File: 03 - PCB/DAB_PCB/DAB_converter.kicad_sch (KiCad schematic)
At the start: 190 parts, among them IC1 UCC27288DR, IC10 INA201AID, IC11 INA201AID, IC12 MCP6241-E_P, IC13 MCP6241-E_P, IC2 UCC27288DR, IC3 UCC27288DR, IC4 UCC27288DR, IC5 UA78L12ACDR, IC6 INA201AID, IC9 INA201AID, J3 N3431-6302RB

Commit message: started routing
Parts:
- added TP19: V', DAB:test point 2, symbol DAB_EE365:root_0_Test point_DAB_EE365.SchLib
- added TP20: I', DAB:test point 2, symbol DAB_EE365:root_0_Test point_DAB_EE365.SchLib
- TP1, TP10, TP11, TP13, TP15, TP2, TP3, TP4, TP5, TP6, TP7, TP8, TP9: footprint Connector_PinHeader_2.54mm:PinHeader_1x02_P2.54mm_Vertical -> DAB:test point 2
- TP12, TP18: footprint (none) -> Connector_PinHeader_2.54mm:PinHeader_1x03_P2.54mm_Vertical
- TP14: value I_prim -> I''; footprint Connector_PinHeader_2.54mm:PinHeader_1x02_P2.54mm_Vertical -> DAB:test point 2
- TP16: value I_sec -> V''; footprint Connector_PinHeader_2.54mm:PinHeader_1x02_P2.54mm_Vertical -> DAB:test point 2
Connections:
- net ADCB1 is gone; now on net V'': TP16.1
- net ADCA1: no longer TP14.1
- net ADCA2: no longer C16.2, R15.1
- net ADCA3: now also C16.2, R15.1
- net GND: now also TP19.2, TP20.2
- net prim+: no longer C21.2, C22.2, PS1.1 (VIN)
- net prim-: now also C21.2, C22.2, PS1.1 (VIN)
- net V'': now reaches IC13.6 (VOUT), R18.2, R20.1
- net V': now reaches IC12.6 (VOUT), R17.2, R19.1
- net V': now also TP19.1
- net I'': now reaches IC11.2 (OUT), R16.2
- net I'': now also TP14.1
- net I': now reaches IC10.2 (OUT), R15.2
- net I': now also TP20.1
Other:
- moved on the sheet: TP14, TP15, TP16

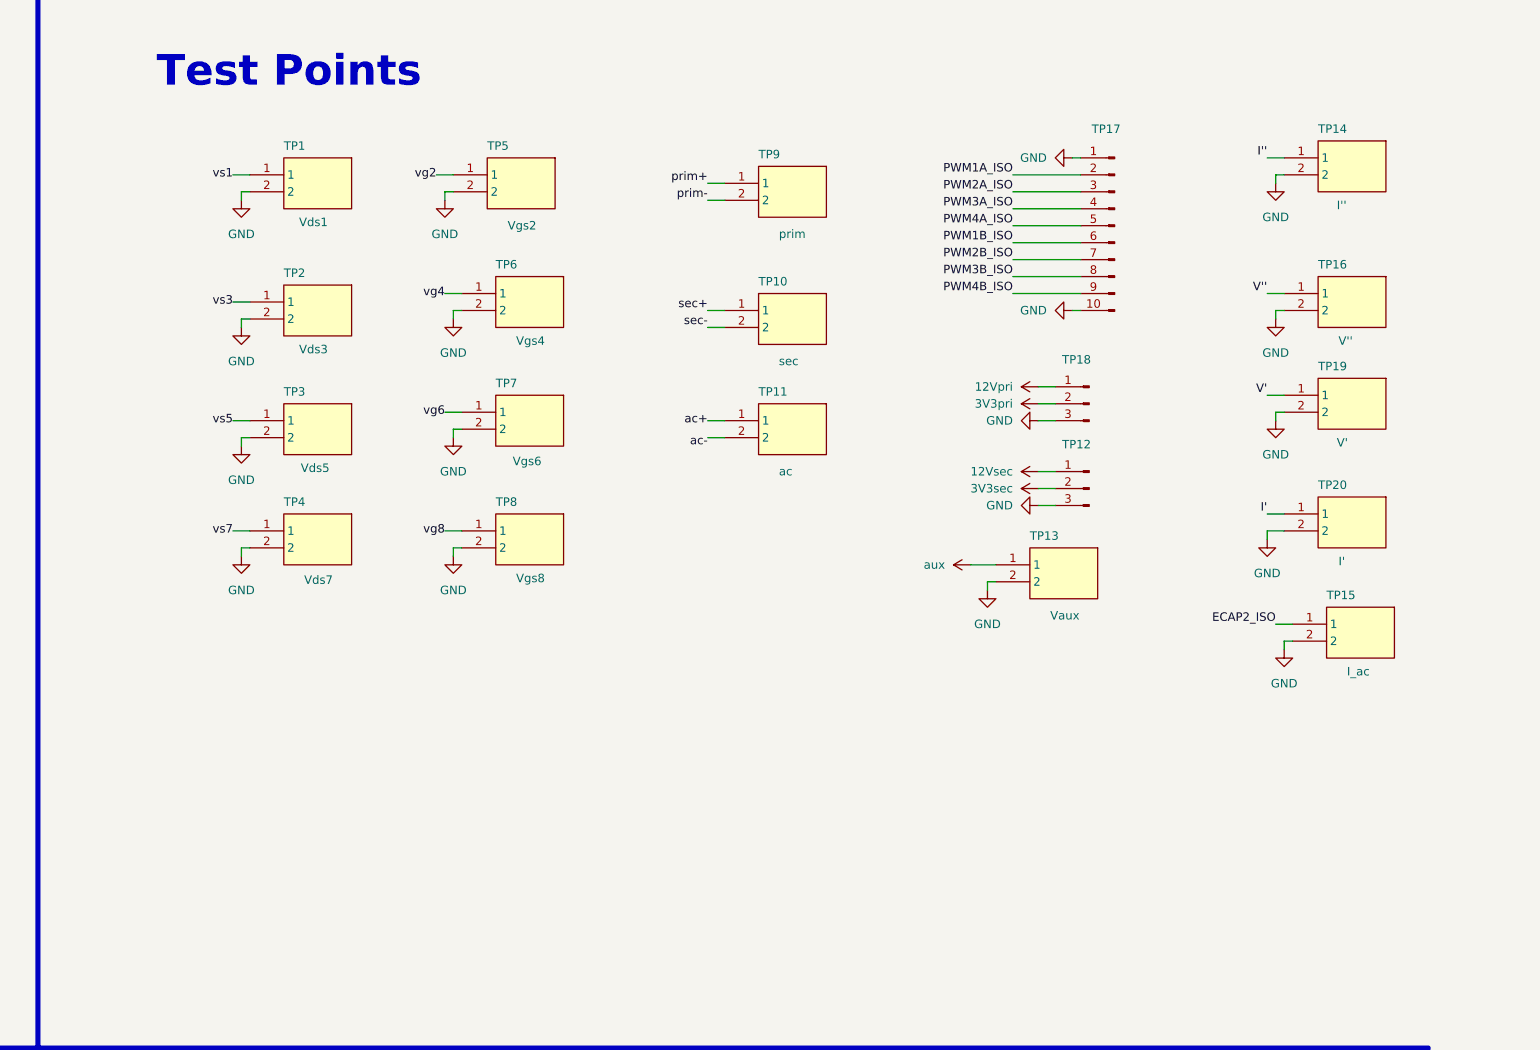
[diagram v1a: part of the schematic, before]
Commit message: added all test points
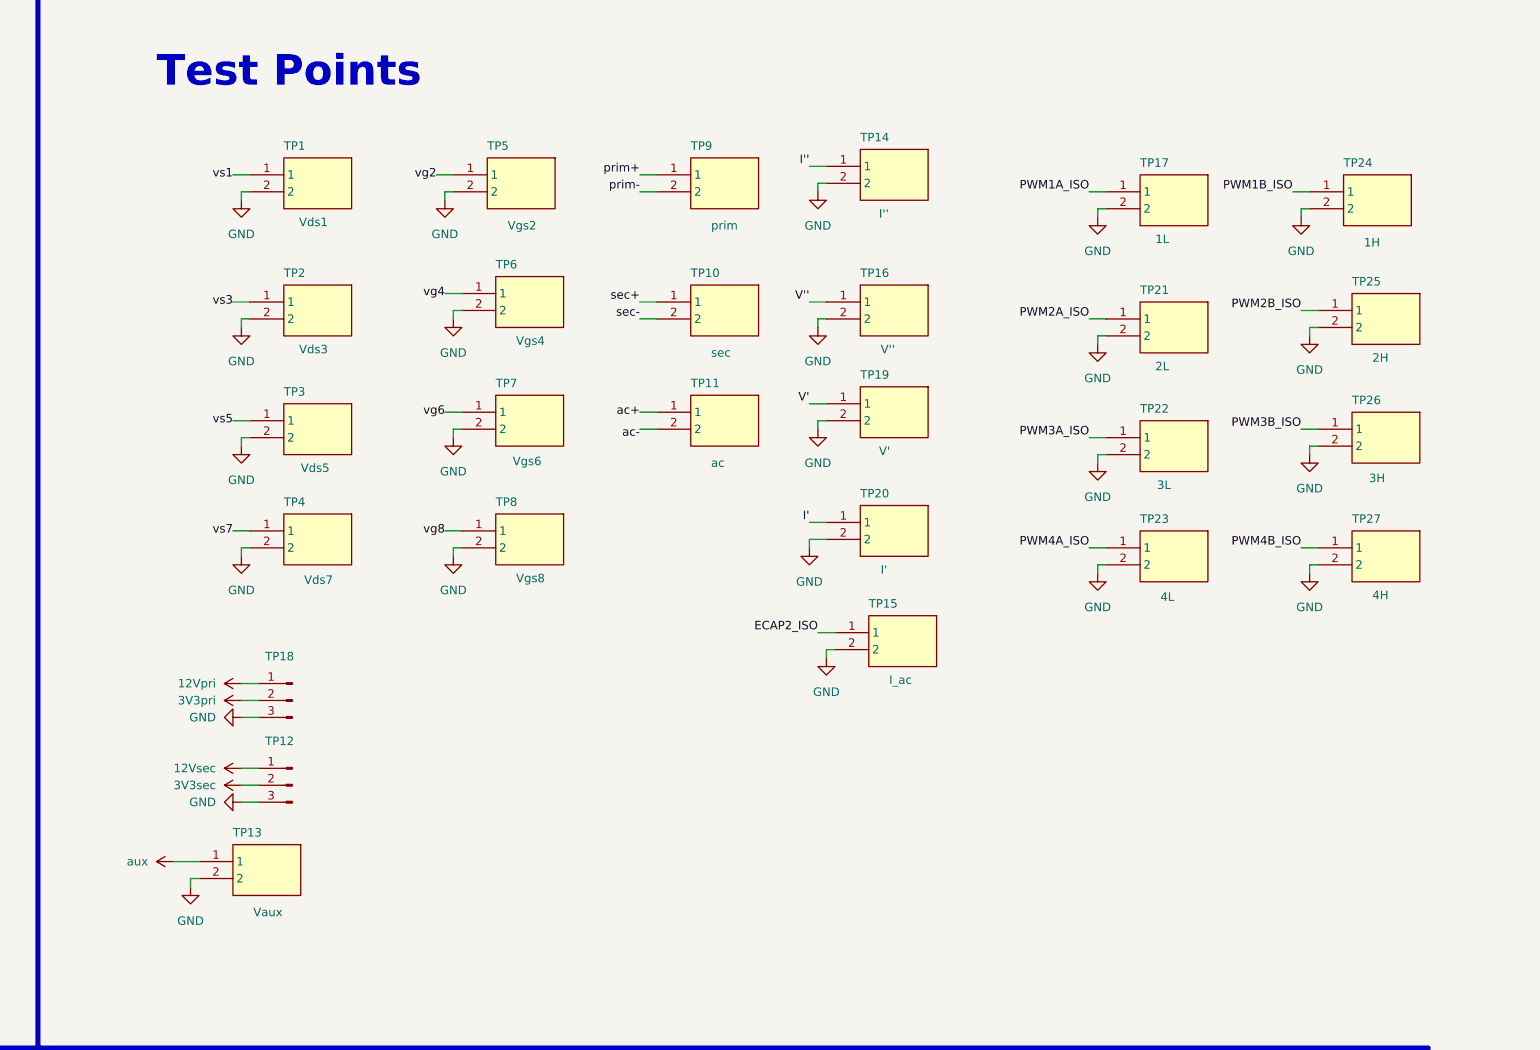
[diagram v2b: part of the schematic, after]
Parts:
- removed TP17: Conn_01x10_Pin, Connector_PinHeader_2.54mm:PinHeader_1x10_P2.54mm_Vertical, symbol Connector:Conn_01x10_Pin
- added TP17: 1L, DAB:test point 2, symbol DAB_EE365:root_0_Test point_DAB_EE365.SchLib
- added TP21: 2L, DAB:test point 2, symbol DAB_EE365:root_0_Test point_DAB_EE365.SchLib
- added TP22: 3L, DAB:test point 2, symbol DAB_EE365:root_0_Test point_DAB_EE365.SchLib
- added TP23: 4L, DAB:test point 2, symbol DAB_EE365:root_0_Test point_DAB_EE365.SchLib
- added TP24: 1H, DAB:test point 2, symbol DAB_EE365:root_0_Test point_DAB_EE365.SchLib
- added TP25: 2H, DAB:test point 2, symbol DAB_EE365:root_0_Test point_DAB_EE365.SchLib
- added TP26: 3H, DAB:test point 2, symbol DAB_EE365:root_0_Test point_DAB_EE365.SchLib
- added TP27: 4H, DAB:test point 2, symbol DAB_EE365:root_0_Test point_DAB_EE365.SchLib
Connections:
- net GND: now also TP17.2, TP21.2, TP22.2, TP23.2, TP24.2, TP25.2, TP26.2, TP27.2
- net PWM1A_ISO: now also TP17.1
- net PWM1B_ISO: now also TP24.1
- net PWM2A_ISO: now also TP21.1
- net PWM2B_ISO: now also TP25.1
- net PWM3A_ISO: now also TP22.1
- net PWM3B_ISO: now also TP26.1
- net PWM4A_ISO: now also TP23.1
- net PWM4B_ISO: now also TP27.1
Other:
- moved on the sheet: TP10, TP11, TP12, TP13, TP14, TP15, TP16, TP18, TP19, TP20, TP9

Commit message: DC-DC
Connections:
- net 12Vpri: no longer C11.2, C6.2, C_vdd3.2, C_vdd4.2, IC15.3 (INPUT), IC3.1 (VDD), IC4.1 (VDD), IC5.1 (OUTPUT), LED2.2 (A), Rboot3.2, Rboot4.2, TP12.1 (Pin_1)
- new net 12Vsec: C11.2, C6.2, C_vdd3.2, C_vdd4.2, IC15.3 (INPUT), IC3.1 (VDD), IC4.1 (VDD), IC5.1 (OUTPUT), LED2.2 (A), Rboot3.2, Rboot4.2, TP12.1 (Pin_1)

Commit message: cleaned up silkscreen
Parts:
- renumbered Dboot1 to D6, Dboot2 to D7, Dboot4 to D8, Dboot3 to D9, SWH1 to Q1, SWH5 to Q2, SWH2 to Q3, SWH7 to Q4, SWH3 to Q5, SWH6 to Q6, SWH4 to Q7, SWH8 to Q8, Rboot1 to R21, Rboot2 to R22, Rboot4 to R23, Rboot3 to R24
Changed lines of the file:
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@@
 		(in_pos_files yes)
 		(dnp no)
-		(property "Reference" "SWH7"
+		(property "Reference" "Q4"
 			(at 260.096 102.616 90)
 			(show_name no)
@@
 			(project "DAB_converter"
 				(path "/10e55807-643b-4bc9-b726-ccd65e076347"
-					(reference "SWH7")
+					(reference "Q4")
 					(unit 1)
 				)
@@
 		(in_pos_files yes)
 		(dnp no)
-		(property "Reference" "SWH6"
+		(property "Reference" "Q6"
 			(at 366.776 101.346 90)
 			(show_name no)
@@
 			(project "DAB_converter"
 				(path "/10e55807-643b-4bc9-b726-ccd65e076347"
-					(reference "SWH6")
+					(reference "Q6")
 					(unit 1)
 				)
@@
 		(in_pos_files yes)
 		(dnp no)
-		(property "Reference" "SWH1"
+		(property "Reference" "Q1"
 			(at 227.076 77.216 90)
 			(show_name no)
@@
 			(project "DAB_converter"
 				(path "/10e55807-643b-4bc9-b726-ccd65e076347"
-					(reference "SWH1")
+					(reference "Q1")
 					(unit 1)
 				)
@@
 		(in_pos_files yes)
 		(dnp no)
-		(property "Reference" "SWH8"
+		(property "Reference" "Q8"
 			(at 399.796 102.616 90)
 			(show_name no)
@@
 			(project "DAB_converter"
 				(path "/10e55807-643b-4bc9-b726-ccd65e076347"
-					(reference "SWH8")
+					(reference "Q8")
 					(unit 1)
 				)
@@
 		(in_pos_files yes)
 		(dnp no)
-		(property "Reference" "SWH4"
+		(property "Reference" "Q7"
 			(at 399.796 77.216 90)
 			(show_name no)
@@
 			(project "DAB_converter"
 				(path "/10e55807-643b-4bc9-b726-ccd65e076347"
-					(reference "SWH4")
+					(reference "Q7")
 					(unit 1)
 				)
@@
 		(in_pos_files yes)
 		(dnp no)
-		(property "Reference" "SWH3"
+		(property "Reference" "Q5"
 			(at 366.776 77.216 90)
 			(show_name no)
@@
 			(project "DAB_converter"
 				(path "/10e55807-643b-4bc9-b726-ccd65e076347"
-					(reference "SWH3")
+					(reference "Q5")
 					(unit 1)
 				)
@@
 		(in_pos_files yes)
 		(dnp no)
-		(property "Reference" "SWH5"
+		(property "Reference" "Q2"
 			(at 227.076 101.346 90)
 			(show_name no)
@@
 			(project "DAB_converter"
 				(path "/10e55807-643b-4bc9-b726-ccd65e076347"
-					(reference "SWH5")
+					(reference "Q2")
 					(unit 1)
 				)
@@
 		(in_pos_files yes)
 		(dnp no)
-		(property "Reference" "Rboot4"
-			(at 483.87 254.508 90)
+		(property "Reference" "R23"
+			(at 486.156 255.016 90)
 			(show_name no)
 			(do_not_autoplace no)
@@
 			(project "DAB_converter"
 				(path "/10e55807-643b-4bc9-b726-ccd65e076347"
-					(reference "Rboot4")
+					(reference "R23")
 					(unit 1)
 				)
@@
 		(in_pos_files yes)
 		(dnp no)
-		(property "Reference" "Dboot1"
+		(property "Reference" "D6"
 			(at 106.68 264.16 0)
 			(show_name no)
@@
 			(project "DAB_converter"
 				(path "/10e55807-643b-4bc9-b726-ccd65e076347"
-					(reference "Dboot1")
+					(reference "D6")
 					(unit 1)
 				)
@@
 		(in_pos_files yes)
 		(dnp no)
-		(property "Reference" "Dboot3"
+		(property "Reference" "D9"
 			(at 623.57 266.7 0)
 			(show_name no)
@@
 			(project "DAB_converter"
 				(path "/10e55807-643b-4bc9-b726-ccd65e076347"
-					(reference "Dboot3")
+					(reference "D9")
 					(unit 1)
 				)
@@
 		(in_pos_files yes)
 		(dnp no)
-		(property "Reference" "SWH2"
+		(property "Reference" "Q3"
 			(at 260.096 77.216 90)
 			(show_name no)
@@
 			(project "DAB_converter"
 				(path "/10e55807-643b-4bc9-b726-ccd65e076347"
-					(reference "SWH2")
+					(reference "Q3")
 					(unit 1)
 				)
@@
 		(in_pos_files yes)
 		(dnp no)
-		(property "Reference" "Rboot3"
-			(at 617.22 253.238 90)
+		(property "Reference" "R24"
+			(at 619.506 253.238 90)
 			(show_name no)
 			(do_not_autoplace no)
@@
 			(project "DAB_converter"
 				(path "/10e55807-643b-4bc9-b726-ccd65e076347"
-					(reference "Rboot3")
+					(reference "R24")
 					(unit 1)
 				)
@@
 		(in_pos_files yes)
 		(dnp no)
-		(property "Reference" "Dboot4"
+		(property "Reference" "D8"
 			(at 490.22 269.24 0)
 			(show_name no)
@@
 			(project "DAB_converter"
 				(path "/10e55807-643b-4bc9-b726-ccd65e076347"
-					(reference "Dboot4")
+					(reference "D8")
 					(unit 1)
 				)
@@
 		(in_pos_files yes)
 		(dnp no)
-		(property "Reference" "Rboot2"
+		(property "Reference" "R22"
 			(at 228.6 250.19 90)
 			(show_name no)
@@
 			(project "DAB_converter"
 				(path "/10e55807-643b-4bc9-b726-ccd65e076347"
-					(reference "Rboot2")
+					(reference "R22")
 					(unit 1)
 				)
@@
 		(in_pos_files yes)
 		(dnp no)
-		(property "Reference" "Dboot2"
+		(property "Reference" "D7"
 			(at 234.95 264.16 0)
 			(show_name no)
@@
 			(project "DAB_converter"
 				(path "/10e55807-643b-4bc9-b726-ccd65e076347"
-					(reference "Dboot2")
+					(reference "D7")
 					(unit 1)
 				)
@@
 		(in_pos_files yes)
 		(dnp no)
-		(property "Reference" "Rboot1"
-			(at 100.076 250.698 90)
+		(property "Reference" "R21"
+			(at 102.616 251.46 90)
 			(show_name no)
 			(do_not_autoplace no)
@@
 			(project "DAB_converter"
 				(path "/10e55807-643b-4bc9-b726-ccd65e076347"
-					(reference "Rboot1")
+					(reference "R21")
 					(unit 1)
 				)
